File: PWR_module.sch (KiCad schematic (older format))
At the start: 18 parts, among them P14 CONN_01X02, P15 FUSE, P16 CONN_01X02, P4 CONN_01X02, T1 TRANSFO, U1 SPX2920M3-3.3, U4 PCB_SWITCH_PSU, U7 SPX2920M3-3.3, U8 SPX2920M3-3.3, U9 SPX2920M3-3.3

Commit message: the version sent to Eurocircuits
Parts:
- removed P15: FUSE, Fuse_Holders_and_Fuses:Fuseholder_Fuse_TR5_Littlefuse-No560_No460, symbol CONN_01X02
- C1: footprint Capacitors_ThroughHole:C_Radial_D16_L31.5_P7.5 -> Capacitors_ThroughHole:C_Radial_D14_L31.5_P5
- C18, C4: footprint Capacitors_ThroughHole:C_Radial_D16_L30_P7.5 -> Capacitors_ThroughHole:C_Radial_D14_L31.5_P5
- P14, P16, P4: footprint libs:PIN_CONN_0.3Inch -> Fuse_Holders_and_Fuses:Fuseholder5x20_horiz_SemiClosed_Casing10x25mm
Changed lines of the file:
@@
 F 0 "C1" H 6425 3100 50  0000 L CNN
 F 1 "CP" H 6425 2900 50  0000 L CNN
-F 2 "Capacitors_ThroughHole:C_Radial_D16_L31.5_P7.5" H 6438 2850 30  0001 C CNN
+F 2 "Capacitors_ThroughHole:C_Radial_D14_L31.5_P5" H 6438 2850 30  0001 C CNN
 F 3 "" H 6400 3000 60  0000 C CNN
 	1    6400 3000
@@
 F 0 "C4" H 8025 3100 50  0000 L CNN
 F 1 "CP" H 8025 2900 50  0000 L CNN
-F 2 "Capacitors_ThroughHole:C_Radial_D16_L30_P7.5" H 8038 2850 30  0001 C CNN
+F 2 "Capacitors_ThroughHole:C_Radial_D14_L31.5_P5" H 8038 2850 30  0001 C CNN
 F 3 "" H 8000 3000 60  0000 C CNN
 	1    8000 3000
@@
 F 0 "C18" H 8125 4450 50  0000 L CNN
 F 1 "CP" H 8125 4250 50  0000 L CNN
-F 2 "Capacitors_ThroughHole:C_Radial_D16_L30_P7.5" H 8138 4200 30  0001 C CNN
+F 2 "Capacitors_ThroughHole:C_Radial_D14_L31.5_P5" H 8138 4200 30  0001 C CNN
 F 3 "" H 8100 4350 60  0000 C CNN
 	1    8100 4350
@@
 F 0 "P14" H 3350 2250 50  0000 C CNN
 F 1 "CONN_01X02" V 3450 2100 50  0000 C CNN
-F 2 "libs:PIN_CONN_0.3Inch" H 3350 2100 60  0000 C CNN
+F 2 "Fuse_Holders_and_Fuses:Fuseholder5x20_horiz_SemiClosed_Casing10x25mm" H 3350 2100 60  0000 C CNN
 F 3 "" H 3350 2100 60  0000 C CNN
 	1    3350 2100
 	-1   0    0    1
-$EndComp
-$Comp
-L CONN_01X02 P15
-U 1 1 5634C69D
-P 3750 2100
-F 0 "P15" H 3750 2250 50  0000 C CNN
-F 1 "FUSE" V 3850 2100 50  0000 C CNN
-F 2 "Fuse_Holders_and_Fuses:Fuseholder_Fuse_TR5_Littlefuse-No560_No460" H 3750 2100 60  0000 C CNN
-F 3 "" H 3750 2100 60  0000 C CNN
-	1    3750 2100
-	1    0    0    -1
 $EndComp
 $Comp
@@
 F 0 "P4" H 2550 2600 50  0000 C CNN
 F 1 "CONN_01X02" V 2650 2450 50  0000 C CNN
-F 2 "libs:PIN_CONN_0.3Inch" H 2550 2450 60  0000 C CNN
+F 2 "Fuse_Holders_and_Fuses:Fuseholder5x20_horiz_SemiClosed_Casing10x25mm" H 2550 2450 60  0000 C CNN
 F 3 "" H 2550 2450 60  0000 C CNN
 	1    2550 2450
@@
 F 0 "P16" H 6200 2800 50  0000 C CNN
 F 1 "CONN_01X02" V 6300 2650 50  0000 C CNN
-F 2 "libs:PIN_CONN_0.3Inch" H 6200 2650 60  0000 C CNN
-F 3 "" H 6200 2650 60  0000 C CNN
+F 2 "Fuse_Holders_and_Fuses:Fuseholder5x20_horiz_SemiClosed_Casing10x25mm" H 6200 2650 60  0000 C CNN
+F 3 "http://www.hestore.hu/prod_10023832.html?pic_id=6294" H 6200 2650 60  0000 C CNN
 	1    6200 2650
 	0    -1   -1   0

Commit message: - this version has a new power supply 5V 15W - new water level sensing using protectbt
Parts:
- removed C1, C18, C4: CP, Capacitors_ThroughHole:C_Radial_D14_L31.5_P5, symbol CP
- removed C17, C19, C2, C3, C5: C, Capacitors_SMD:C_1206_HandSoldering, symbol C
- removed P14, P4: CONN_01X02, Fuse_Holders_and_Fuses:Fuseholder5x20_horiz_SemiClosed_Casing10x25mm, symbol CONN_01X02
- removed T1: TRANSFO, libs:MYRRA44050_IsolationTransformer, symbol TRANSFO
- removed U1, U8: SPX2920M3-3.3, Transistors_TO-220:TO-220_Neutral123_Vertical_LargePads, symbol SPX2920M3-3.3
- removed U4: PCB_SWITCH_PSU, libs:VTX_214_010_109_AC_DC_PCB_Mount_Power_Supply, symbol PCB_SWITCH_PSU
- removed U7, U9: SPX2920M3-3.3, libs:SOT223-ti-pin2is4too, symbol SPX2920M3-3.3
- added DC/DC_Converter?: OKI-78SR-3.3/1.5-W36-C, water:OKI-78SR-3.3-1.5-W36-C, symbol OKI-78SR-3.3/1.5-W36-C
- added PWR_AC/DC_+!2V: KMS-15A-5, water:VTX-214-015-112, symbol VTX-214-015-112
- P16: footprint Fuse_Holders_and_Fuses:Fuseholder5x20_horiz_SemiClosed_Casing10x25mm -> (none)
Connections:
- net labels added: 230V_AC+, 230V_GND, 230V_NEUTRAL, GND
- net labels removed: 230VNULL, 230VNULL_AFTER, 230VPHASE, 230VPHASE_AFTER, 9V, AC+, AC-, GNDREF
- wire segments 26 -> 1
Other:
- moved on the sheet: P16

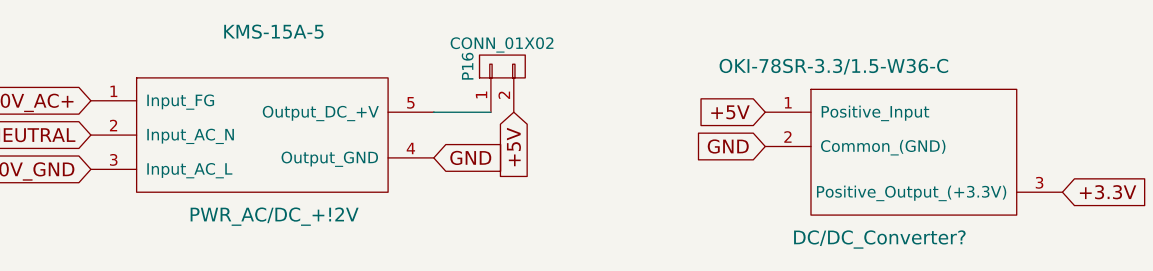
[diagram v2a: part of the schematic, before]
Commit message: - snubber circuit added - diodes selected
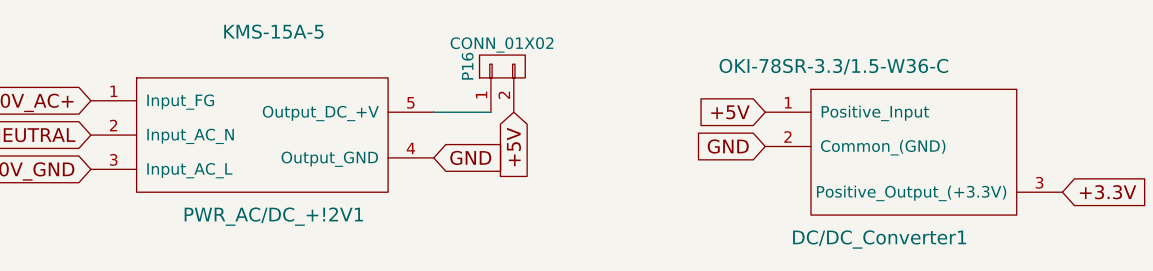
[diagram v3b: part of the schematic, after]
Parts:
- gave numbers to parts that had none: 1
- renumbered PWR_AC/DC_+!2V to PWR_AC/DC_+!2V1
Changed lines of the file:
@@
 F 0 "P16" H 6200 2950 50  0000 C CNN
 F 1 "CONN_01X02" V 6300 2800 50  0000 C CNN
-F 2 "" H 5800 -450 60  0000 C CNN
+F 2 "" H 5800 -450 60  0001 C CNN
 F 3 "" H 6200 1800 60  0000 C CNN
 	1    6200 2800
@@
 $EndComp
 $Comp
-L VTX-214-015-112 PWR_AC/DC_+!2V
+L VTX-214-015-112 PWR_AC/DC_+!2V1
 U 1 1 592449E7
 P 5200 2650
-F 0 "PWR_AC/DC_+!2V" H 5200 1850 60  0000 C CNN
+F 0 "PWR_AC/DC_+!2V1" H 5200 1850 60  0000 C CNN
 F 1 "KMS-15A-5" H 5200 2650 60  0000 C CNN
 F 2 "water:VTX-214-015-112" H 5200 2650 60  0001 C CNN
@@
 +5V
 $Comp
-L OKI-78SR-3.3/1.5-W36-C DC/DC_Converter?
+L OKI-78SR-3.3/1.5-W36-C DC/DC_Converter1
 U 1 1 5925452C
 P 7650 2800
-F 0 "DC/DC_Converter?" H 7850 2050 60  0000 C CNN
+F 0 "DC/DC_Converter1" H 7850 2050 60  0000 C CNN
 F 1 "OKI-78SR-3.3/1.5-W36-C" H 7650 2800 60  0000 C CNN
 F 2 "water:OKI-78SR-3.3-1.5-W36-C" H 7650 2800 60  0001 C CNN

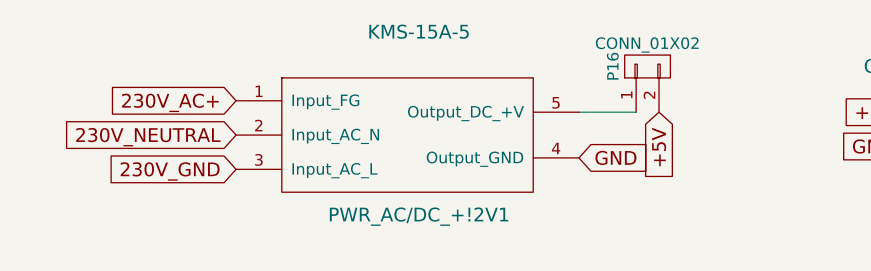
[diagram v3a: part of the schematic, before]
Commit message: all components verified, pcb design required
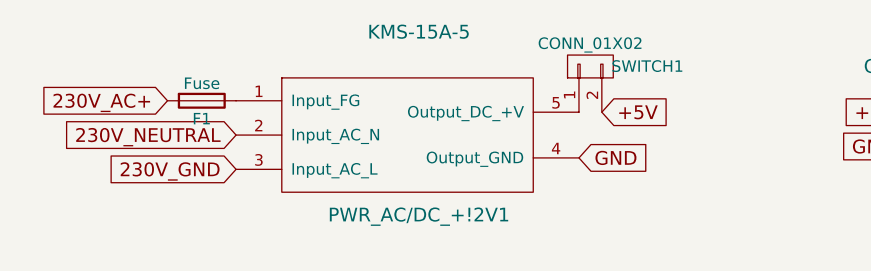
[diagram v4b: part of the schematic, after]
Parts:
- removed P16: CONN_01X02, symbol CONN_01X02
- added F1: Fuse, water:FUSE-0031.8201, symbol Fuse
- added SWITCH1: CONN_01X02, Connectors:GS2, symbol CONN_01X02
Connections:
- net +5V: now also SWITCH1.2 (P2)
- net 230V_AC+: now also F1.2; no longer PWR_AC/DC_+!2V1.1 (Input_FG)
- net at PWR_AC/DC_+!2V1.5 (Output_DC_+V): now also SWITCH1.1 (P1)
- new net: F1.1, PWR_AC/DC_+!2V1.1 (Input_FG)
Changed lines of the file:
@@
 Comment4 ""
 $EndDescr
-Text GLabel 4400 2950 0    60   Input ~ 0
+Text GLabel 4100 2950 0    60   Input ~ 0
 230V_AC+
 Text GLabel 4400 3250 0    60   Input ~ 0
 230V_GND
-$Comp
-L CONN_01X02 P16
-U 1 1 56CE1D02
-P 6200 2800
-F 0 "P16" H 6200 2950 50  0000 C CNN
-F 1 "CONN_01X02" V 6300 2800 50  0000 C CNN
-F 2 "" H 5800 -450 60  0001 C CNN
-F 3 "" H 6200 1800 60  0000 C CNN
-	1    6200 2800
-	0    -1   -1   0
-$EndComp
 $Comp
 L VTX-214-015-112 PWR_AC/DC_+!2V1
@@
 Text GLabel 5900 3200 2    60   Input ~ 0
 GND
-Wire Wire Line
-	5900 3000 6150 3000
 Text GLabel 4400 3100 0    60   Input ~ 0
 230V_NEUTRAL
-Text GLabel 6250 3000 3    60   Input ~ 0
+Text GLabel 6000 3000 2    60   Input ~ 0
 +5V
 $Comp
@@
 Text GLabel 8650 3350 2    60   Input ~ 0
 +3.3V
+$Comp
+L CONN_01X02 SWITCH1
+U 1 1 592C9159
+P 5950 2800
+F 0 "SWITCH1" V 5950 2550 50  0000 C CNN
+F 1 "CONN_01X02" V 6050 2800 50  0000 C CNN
+F 2 "Connectors:GS2" H 5950 2800 50  0001 C CNN
+F 3 "" H 5950 2800 50  0001 C CNN
+	1    5950 2800
+	0    -1   -1   0
+$EndComp
+$Comp
+L Fuse F1
+U 1 1 592CAA69
+P 4250 2950
+F 0 "F1" V 4330 2950 50  0000 C CNN
+F 1 "Fuse" V 4175 2950 50  0000 C CNN
+F 2 "water:FUSE-0031.8201" V 4180 2950 50  0001 C CNN
+F 3 "http://hu.farnell.com/schurter/0031-8201/fuse-holder-pcb-20x5mm/dp/1162740" H 4250 2950 50  0001 C CNN
+	1    4250 2950
+	0    1    1    0
+$EndComp
 $EndSCHEMATC

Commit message: this version has the parts organized; before routing
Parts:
- SWITCH1: footprint Connectors:GS2 -> Connectors:PINHEAD1-2
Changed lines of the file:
@@
 F 0 "SWITCH1" V 5950 2550 50  0000 C CNN
 F 1 "CONN_01X02" V 6050 2800 50  0000 C CNN
-F 2 "Connectors:GS2" H 5950 2800 50  0001 C CNN
+F 2 "Connectors:PINHEAD1-2" H 5950 2800 50  0001 C CNN
 F 3 "" H 5950 2800 50  0001 C CNN
 	1    5950 2800

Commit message: updated links
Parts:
- PWR_AC/DC_+!2V1: alternative cheap (none) -> http://hu.farnell.com/vigortronix/vtx-214-010-205/power-sup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
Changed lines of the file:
@@
 F 2 "water:VTX-214-015-112" H 5200 2650 60  0001 C CNN
 F 3 "http://hu.farnell.com/tdk-lambda/kms-15a-5/power-supply-ac-dc-5v-3a/dp/2664694" H 5200 2650 60  0001 C CNN
+F 4 "http://hu.farnell.com/vigortronix/vtx-214-010-205/power-supply-ac-dc-5v-2a/dp/2464685" H 5200 2650 60  0001 C CNN "alternative cheap"
 	1    5200 2650
 	1    0    0    -1

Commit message: stash commit before the revision of the parts
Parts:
- DC/DC_Converter1: small power 0.5A (none) -> http://hu.farnell.com/texas-instruments/ua78m33qdcyrg4q1/li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
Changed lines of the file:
@@
 F 2 "water:OKI-78SR-3.3-1.5-W36-C" H 7650 2800 60  0001 C CNN
 F 3 "http://hu.farnell.com/murata-power-solutions/oki-78sr-3-3-1-5-w36-c/sr-dc-dc-converter-sip-module/dp/2102100" H 7650 2800 60  0001 C CNN
+F 4 "http://hu.farnell.com/texas-instruments/ua78m33qdcyrg4q1/linear-voltreg-3-3v-0-5a-sot-223/dp/2463957?ost=2463957&searchView=table&iscrfnonsku=false&ddkey=http%3Ahu-HU%2FElement14_Hungary%2Fsearch" H 7650 2800 60  0001 C CNN "small power 0.5A"
 	1    7650 2800
 	1    0    0    -1
@@
 	0    1    1    0
 $EndComp
+Text Label 7700 3950 0    60   ~ 0
+CHECK!!!
 $EndSCHEMATC
